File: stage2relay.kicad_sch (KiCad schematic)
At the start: 5 parts, among them SW2 SW_Push

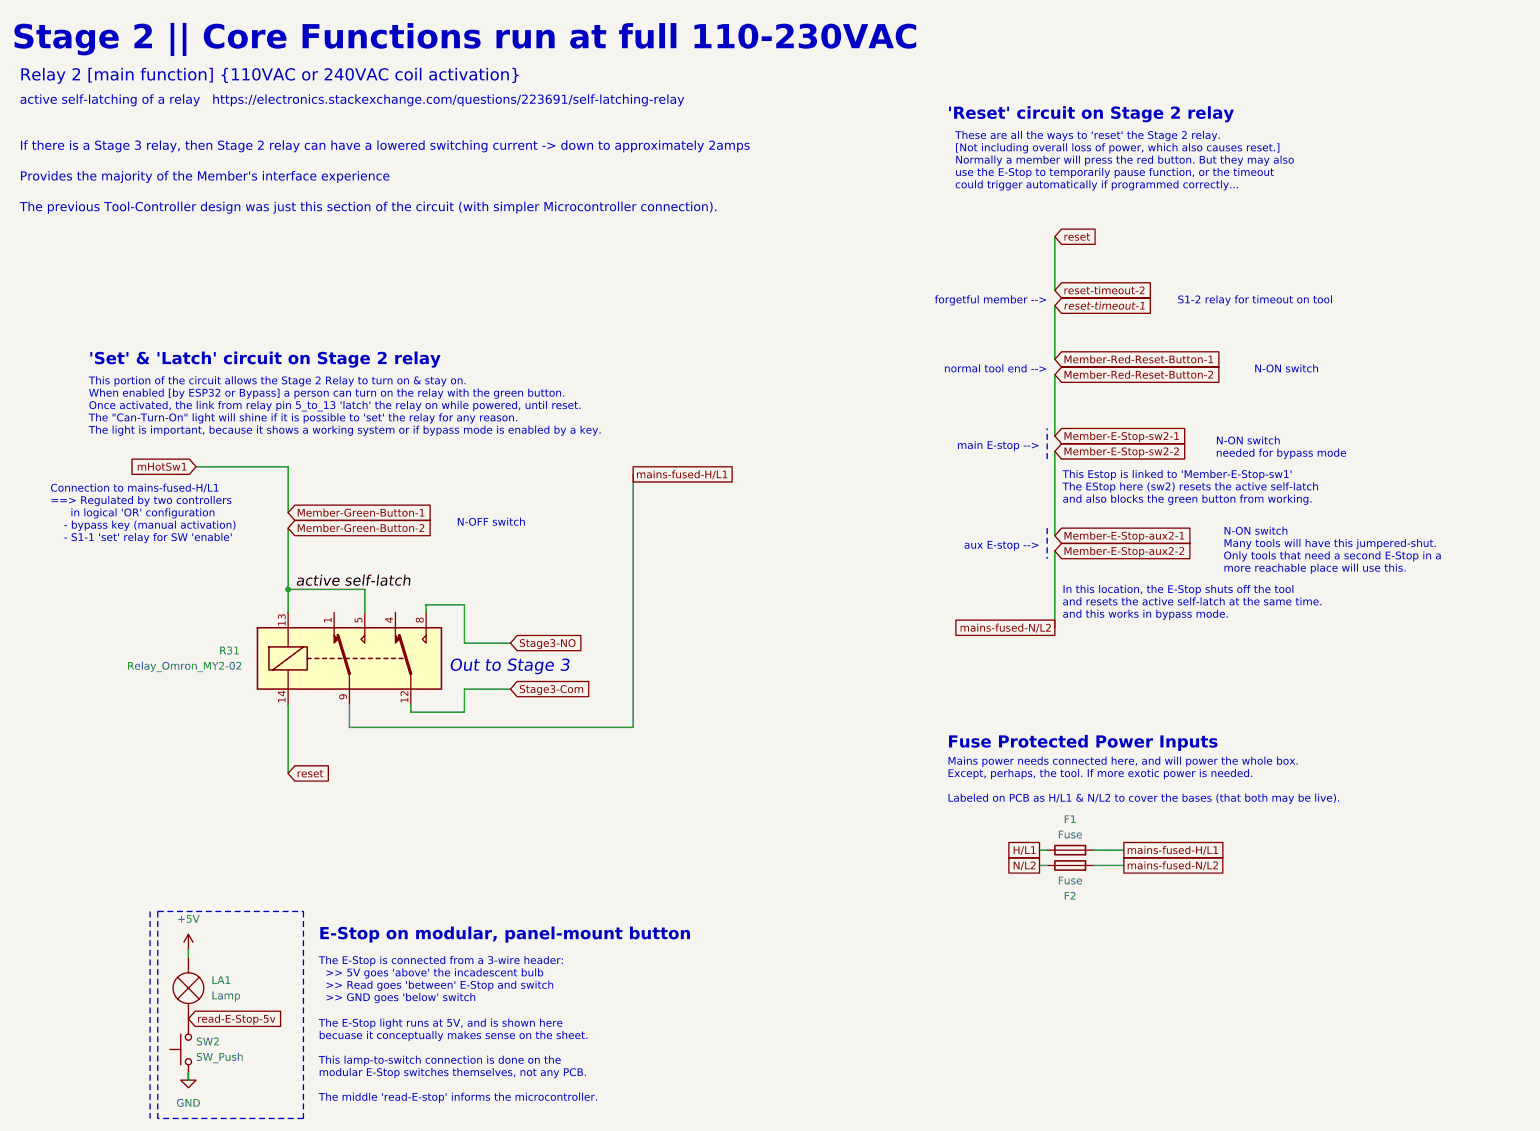
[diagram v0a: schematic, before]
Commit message: double-check mains connections, update notes
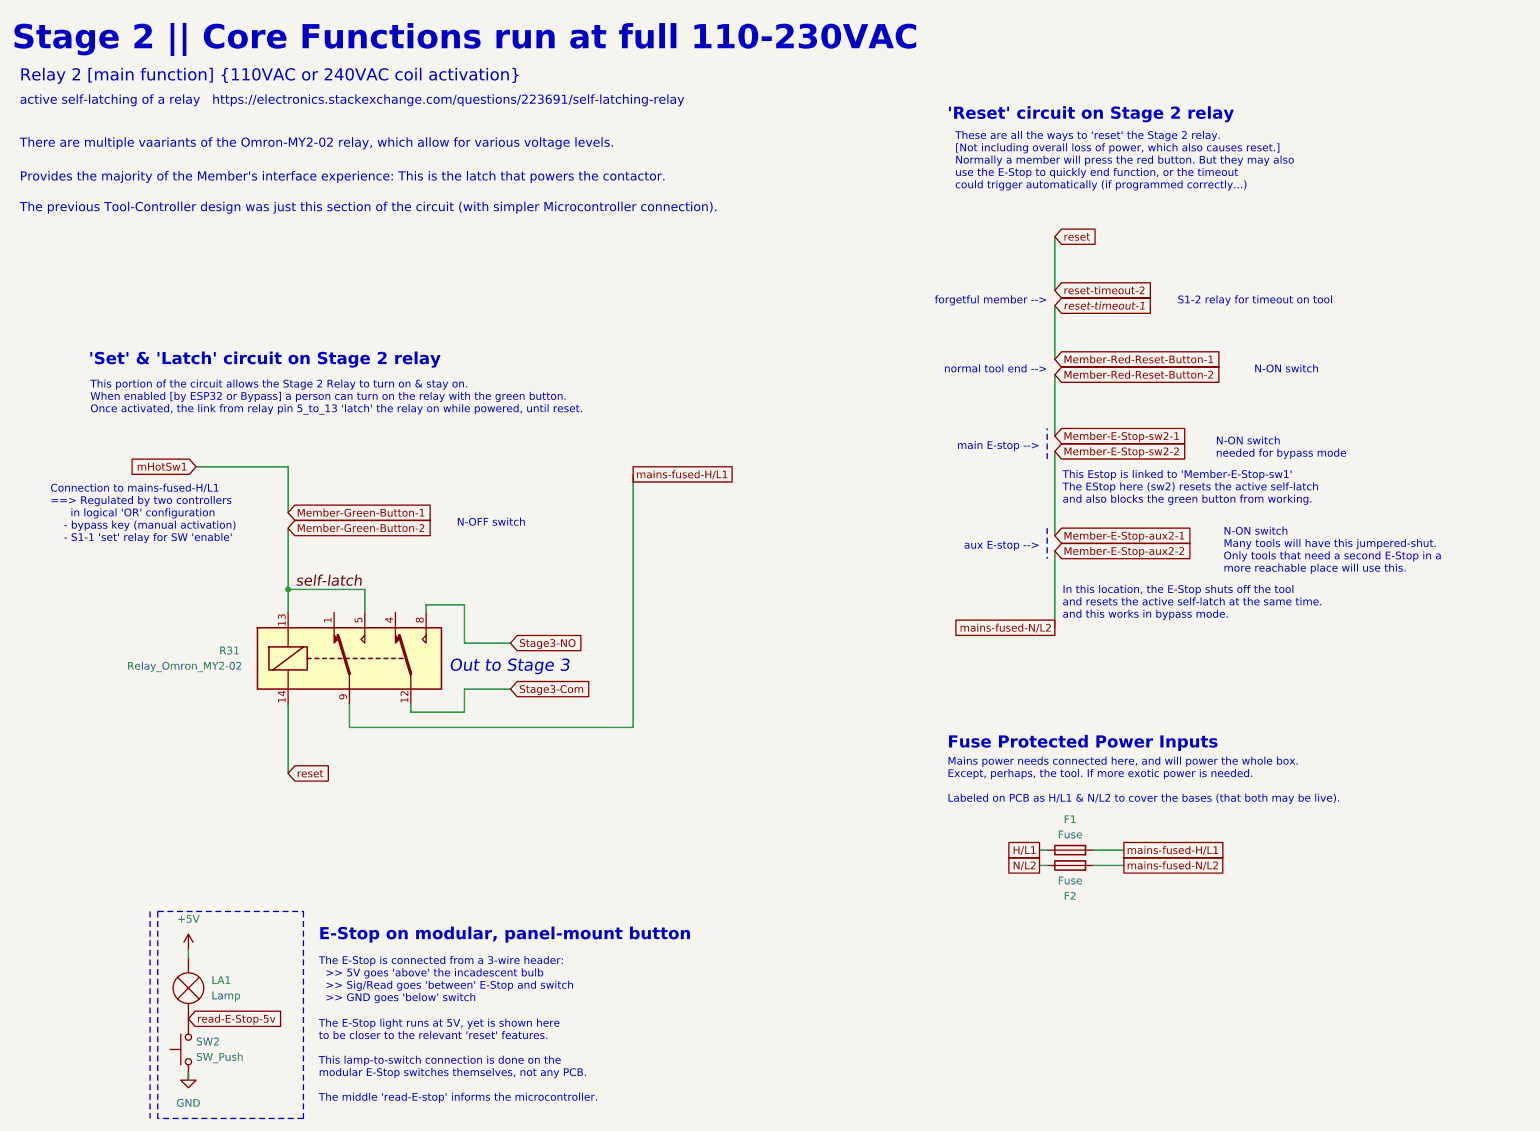
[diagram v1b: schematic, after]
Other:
- note added: "Provides the majority of the Member's interface experience: This is the latch that powers the contactor."
- note added: "The E-Stop is connected from a 3-wire header: >> 5V goes 'above' the incadescent bulb >> Sig/Read goes 'between' E-Stop and switch >> GND goes 'below' switch"
- note added: "The E-Stop light runs at 5V, yet is shown here to be closer to the relevant 'reset' features. This lamp-to-switch connection is done on the modular E-Stop switches themselves, not any PCB. The middle 'read-E-stop' informs the microcontroller."
- note added: "There are multiple vaariants of the Omron-MY2-02 relay, which allow for various voltage levels."
- note added: "These are all the ways to 'reset' the Stage 2 relay. [Not including overall loss of power, which also causes reset.] Normally a member will press the red button. But they may also use the E-Stop to quickly end function, or the timeout could trigger automatically (if programmed correctly...)"
- note added: "This portion of the circuit allows the Stage 2 Relay to turn on & stay on. When enabled [by ESP32 or Bypass] a person can turn on the relay with the green button. Once activated, the link from relay pin 5_to_13 'latch' the relay on while powered, until reset."
- note removed: "If there is a Stage 3 relay, then Stage 2 relay can have a lowered switching current -> down to approximately 2amps"
- note removed: "Provides the majority of the Member's interface experience"
- note removed: "The E-Stop is connected from a 3-wire header: >> 5V goes 'above' the incadescent bulb >> Read goes 'between' E-Stop and switch >> GND goes 'below' switch"
- note removed: "The E-Stop light runs at 5V, and is shown here becuase it conceptually makes sense on the sheet. This lamp-to-switch connection is done on the modular E-Stop switches themselves, not any PCB. The middle 'read-E-stop' informs the microcontroller."
- note removed: "These are all the ways to 'reset' the Stage 2 relay. [Not including overall loss of power, which also causes reset.] Normally a member will press the red button. But they may also use the E-Stop to temporarily pause function, or the timeout could trigger automatically if programmed correctly..."
- note removed: "This portion of the circuit allows the Stage 2 Relay to turn on & stay on. When enabled [by ESP32 or Bypass] a person can turn on the relay with the green button. Once activated, the link from relay pin 5_to_13 'latch' the relay on while powered, until reset. The "Can-Turn-On" light will shine if it is possible to 'set' the relay for any reason. The light is important, because it shows a working 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"
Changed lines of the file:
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@@
 		(rev "3")
 		(company "Corey Rice & MakeHaven")
-		(comment 1 "Once activated, relay holds itself open with power ")
+		(comment 1 "Once activated, relay holds itself in an active state until reset")
 		(comment 2 "Can be interrupted by E-Stops or the S1/'reset' relay")
 		(comment 3 "Fuses added to power inputs, to protect board from improper wiring")
@@
 		)
 	)
-	(text "If there is a Stage 3 relay, then Stage 2 relay can have a lowered switching current -> down to approximately 2amps"
-		(exclude_from_sim no)
-		(at 21.59 38.1 0)
+	(text "The E-Stop light runs at 5V, yet is shown here\nto be closer to the relevant 'reset' features.\n\nThis lamp-to-switch connection is done on the \nmodular E-Stop switches themselves, not any PCB. \n\nThe middle 'read-E-stop' informs the microcontroller."
+		(exclude_from_sim no)
+		(at 71.12 195.58 0)
+		(effects
+			(font
+				(size 1.27 1.27)
+			)
+			(justify left bottom)
+		)
+	)
+	(text "There are multiple vaariants of the Omron-MY2-02 relay, which allow for various voltage levels."
+		(exclude_from_sim no)
+		(at 21.59 37.592 0)
 		(effects
 			(font
@@
 		)
 	)
-	(text "The E-Stop light runs at 5V, and is shown here\nbecuase it conceptually makes sense on the sheet.\n\nThis lamp-to-switch connection is done on the \nmodular E-Stop switches themselves, not any PCB. \n\nThe middle 'read-E-stop' informs the microcontroller."
-		(exclude_from_sim no)
-		(at 71.12 195.58 0)
-		(effects
-			(font
-				(size 1.27 1.27)
-			)
-			(justify left bottom)
-		)
-	)
 	(text "N-ON switch"
 		(exclude_from_sim no)
@@
 		)
 	)
-	(text "The E-Stop is connected from a 3-wire header:\n  >> 5V goes 'above' the incadescent bulb\n  >> Read goes 'between' E-Stop and switch\n  >> GND goes 'below' switch"
+	(text "The E-Stop is connected from a 3-wire header:\n  >> 5V goes 'above' the incadescent bulb\n  >> Sig/Read goes 'between' E-Stop and switch\n  >> GND goes 'below' switch"
 		(exclude_from_sim no)
 		(at 71.12 179.07 0)
@@
 	(text "aux E-stop -->"
 		(exclude_from_sim no)
-		(at 190.5 104.14 180)
+		(at 190.5 104.14 0)
 		(effects
 			(font
@@
 	(text "forgetful member -->"
 		(exclude_from_sim no)
-		(at 191.77 63.5 180)
+		(at 191.77 63.5 0)
 		(effects
 			(font
@@
 		)
 	)
-	(text "These are all the ways to 'reset' the Stage 2 relay. \n[Not including overall loss of power, which also causes reset.]\nNormally a member will press the red button. But they may also \nuse the E-Stop to temporarily pause function, or the timeout \ncould trigger automatically if programmed correctly..."
+	(text "These are all the ways to 'reset' the Stage 2 relay. \n[Not including overall loss of power, which also causes reset.]\nNormally a member will press the red button. But they may also \nuse the E-Stop to quickly end function, or the timeout \ncould trigger automatically (if programmed correctly...)"
 		(exclude_from_sim no)
 		(at 176.53 44.45 0)
@@
 	(text "normal tool end -->"
 		(exclude_from_sim no)
-		(at 191.77 74.93 180)
+		(at 191.77 74.93 0)
 		(effects
 			(font
@@
 	(text "main E-stop -->"
 		(exclude_from_sim no)
-		(at 190.5 87.63 180)
+		(at 190.5 87.63 0)
 		(effects
 			(font
@@
 		)
 	)
-	(text "Provides the majority of the Member's interface experience\n"
+	(text "Provides the majority of the Member's interface experience: This is the latch that powers the contactor.\n"
 		(exclude_from_sim no)
 		(at 21.59 43.18 0)
@@
 		)
 	)
-	(text "This portion of the circuit allows the Stage 2 Relay to turn on & stay on.\nWhen enabled [by ESP32 or Bypass] a person can turn on the relay with the green button.\nOnce activated, the link from relay pin 5_to_13 'latch' the relay on while powered, until reset.\nThe \"Can-Turn-On\" light will shine if it is possible to 'set' the relay for any reason.\nThe light is important, because it shows a working system or if bypass mode is enabled by a key."
-		(exclude_from_sim no)
-		(at 33.02 85.09 0)
-		(effects
-			(font
-				(size 1.27 1.27)
-			)
-			(justify left bottom)
-		)
-	)
-	(label "active self-latch"
+	(text "This portion of the circuit allows the Stage 2 Relay to turn on & stay on.\nWhen enabled [by ESP32 or Bypass] a person can turn on the relay with the green button.\nOnce activated, the link from relay pin 5_to_13 'latch' the relay on while powered, until reset."
+		(exclude_from_sim no)
+		(at 33.274 81.534 0)
+		(effects
+			(font
+				(size 1.27 1.27)
+			)
+			(justify left bottom)
+		)
+	)
+	(label "self-latch"
 		(at 67.31 110.49 0)
 		(fields_autoplaced yes)
@@
 		)
 		(instances
-			(project "mh-custom-v1.3"
+			(project "wing-combo"
 				(path "/586efc0f-7de2-49a7-ac21-ecfef2f716d6/6f44f9bb-3a88-498d-9739-be3794f35f17/fd75559e-77bb-4f15-bd9f-e39243a04df3"
 					(reference "R31")
@@
 		)
 		(instances
-			(project "mh-custom-v1.3"
+			(project "wing-combo"
 				(path "/586efc0f-7de2-49a7-ac21-ecfef2f716d6/6f44f9bb-3a88-498d-9739-be3794f35f17/fd75559e-77bb-4f15-bd9f-e39243a04df3"
 					(reference "F2")
@@
 		)
 		(instances
-			(project "mh-custom-v1.3"
+			(project "wing-combo"
 				(path "/586efc0f-7de2-49a7-ac21-ecfef2f716d6/6f44f9bb-3a88-498d-9739-be3794f35f17/fd75559e-77bb-4f15-bd9f-e39243a04df3"
 					(reference "#PWR0163")
@@
 		)
 		(instances
-			(project "mh-custom-v1.3"
+			(project "wing-combo"
 				(path "/586efc0f-7de2-49a7-ac21-ecfef2f716d6/6f44f9bb-3a88-498d-9739-be3794f35f17/fd75559e-77bb-4f15-bd9f-e39243a04df3"
 					(reference "F1")
@@
 		)
 		(instances
-			(project "mh-custom-v1.3"
+			(project "wing-combo"
 				(path "/586efc0f-7de2-49a7-ac21-ecfef2f716d6/6f44f9bb-3a88-498d-9739-be3794f35f17/fd75559e-77bb-4f15-bd9f-e39243a04df3"
 					(reference "#PWR0164")
@@
 		)
 		(instances
-			(project "mh-custom-v1.3"
+			(project "wing-combo"
 				(path "/586efc0f-7de2-49a7-ac21-ecfef2f716d6/6f44f9bb-3a88-498d-9739-be3794f35f17/fd75559e-77bb-4f15-bd9f-e39243a04df3"
 					(reference "SW2")
@@
 		)
 		(instances
-			(project "mh-custom-v1.3"
+			(project "wing-combo"
 				(path "/586efc0f-7de2-49a7-ac21-ecfef2f716d6/6f44f9bb-3a88-498d-9739-be3794f35f17/fd75559e-77bb-4f15-bd9f-e39243a04df3"
 					(reference "LA1")

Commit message: fixed j151 relay footprint...probably. also ordered physical relays to confirm
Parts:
- R31: footprint MY2-02 AC110 Omron:relay-Omron-MY2-02 -> J1512CP120VAC1.2_relay:relay-J1512CP120VAC
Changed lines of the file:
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@@
 			)
 		)
-		(property "Footprint" "MY2-02 AC110 Omron:relay-Omron-MY2-02"
+		(property "Footprint" "J1512CP120VAC1.2_relay:relay-J1512CP120VAC"
 			(at 74.93 101.6 0)
 			(effects

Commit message: convert to new parts on the board: footprint change for relay and wishlist-JST connectors
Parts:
- R31: footprint J1512CP120VAC1.2_relay:relay-J1512CP120VAC -> j1512cp120vac1.2:relay-J1512CP120VAC; now left out of the parts list
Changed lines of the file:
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@@
 		(unit 1)
 		(exclude_from_sim no)
-		(in_bom yes)
+		(in_bom no)
 		(on_board yes)
 		(dnp no)
@@
 			)
 		)
-		(property "Footprint" "J1512CP120VAC1.2_relay:relay-J1512CP120VAC"
+		(property "Footprint" "j1512cp120vac1.2:relay-J1512CP120VAC"
 			(at 74.93 101.6 0)
 			(effects

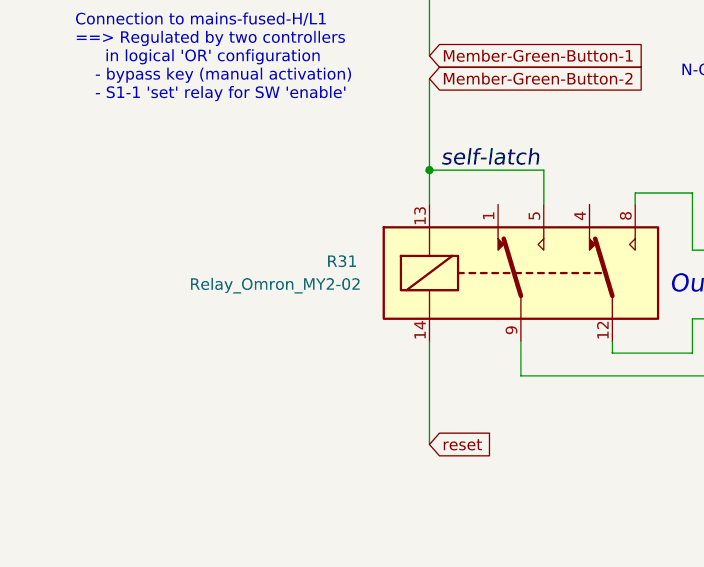
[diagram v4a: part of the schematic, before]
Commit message: added 3D models to design
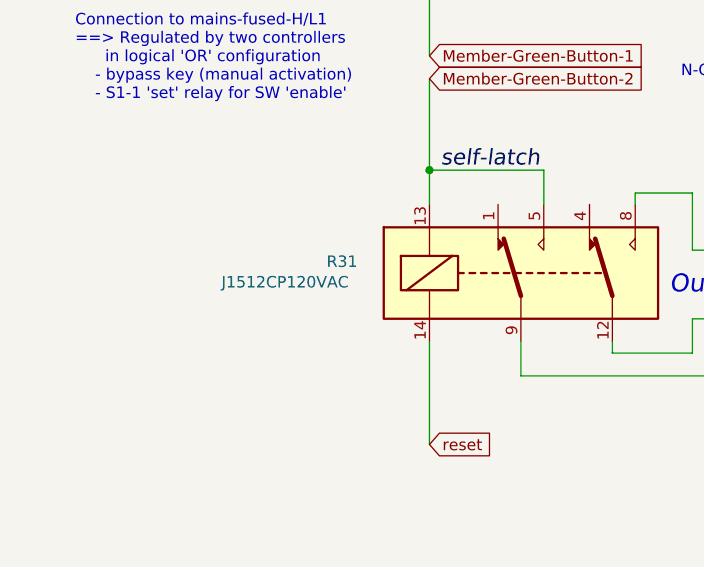
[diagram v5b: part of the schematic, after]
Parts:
- R31: value Relay_Omron_MY2-02 -> J1512CP120VAC
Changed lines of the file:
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@@
 			)
 		)
-		(property "Value" "Relay_Omron_MY2-02"
-			(at 39.37 123.19 0)
+		(property "Value" "J1512CP120VAC"
+			(at 42.926 122.936 0)
 			(effects
 				(font
